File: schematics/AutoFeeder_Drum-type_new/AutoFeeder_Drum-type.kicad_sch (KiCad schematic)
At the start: 35 parts, among them J1 USB_C_Receptacle_6, J2 Conn_02x03_Odd_Even, J3 Conn_01x05, J4 Conn_02x02_Odd_Even, J5 Conn_02x03_Odd_Even, M1 Motor_DC, SW1 SW_SPDT_AND_Push, SW2 SW_DPDT_x2, SW3 SW_DPDT_x2, U1 NJL5901AR-1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

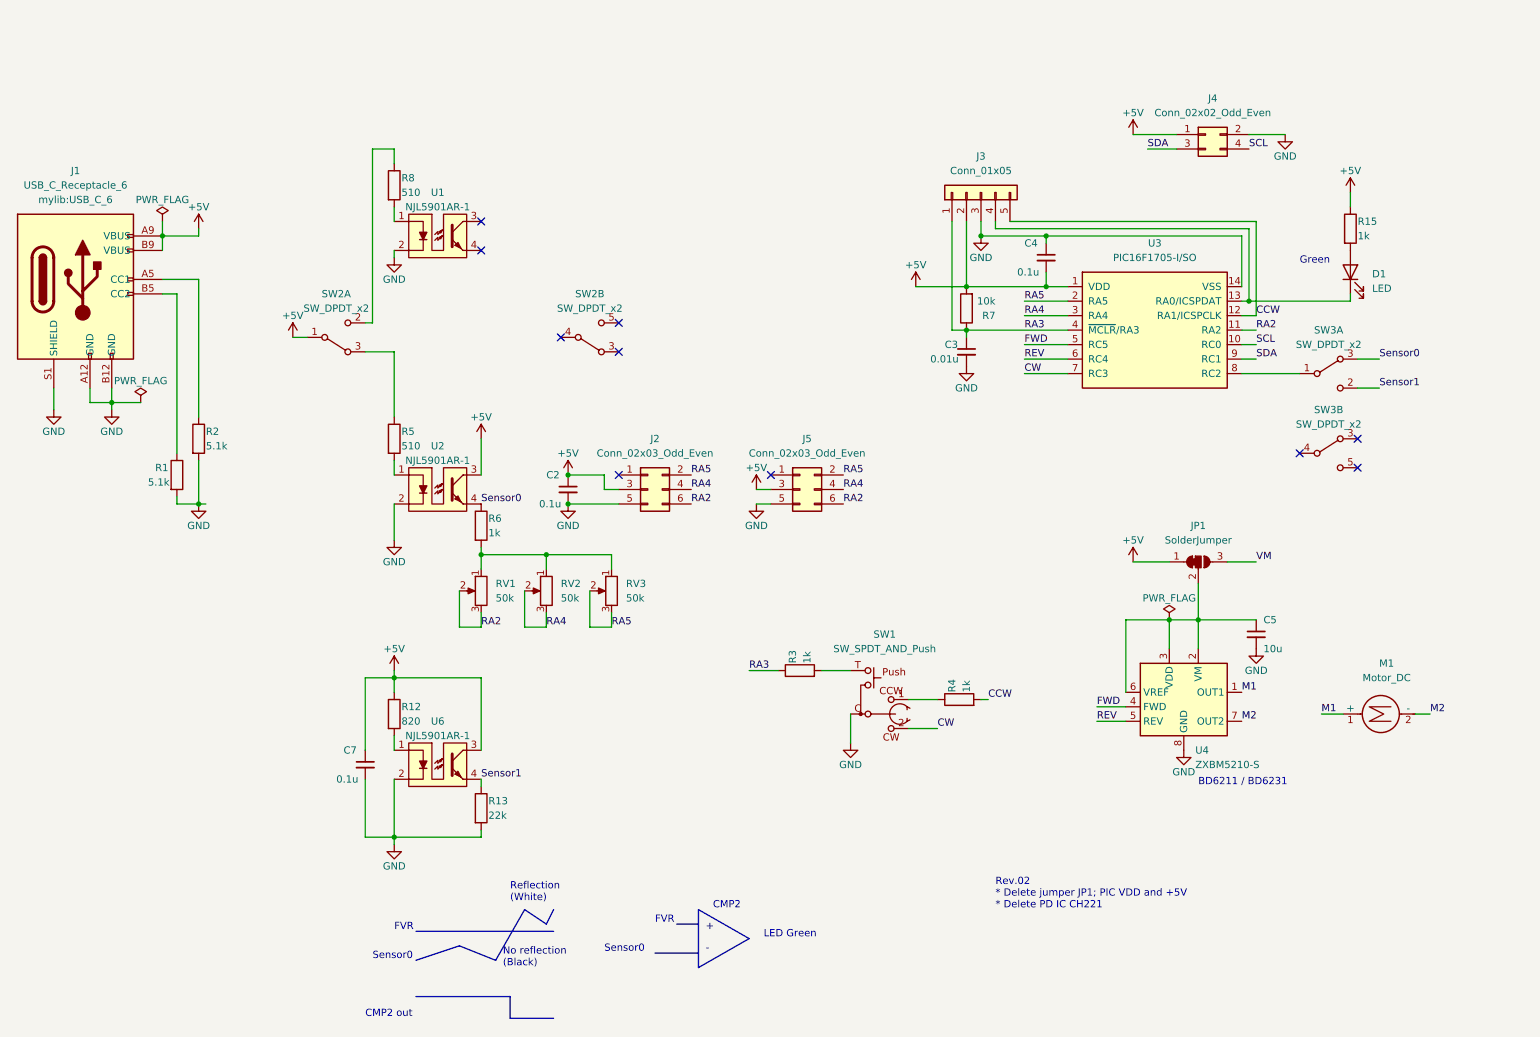
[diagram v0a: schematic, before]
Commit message: Rev.02: Rev01 had a problem with the deep feeder hitting the PCB. Rev02 avoided this problem by overlapping two PCBs for the sensor section.; Three sensitivity options are available for white, transparent, and black feeders.
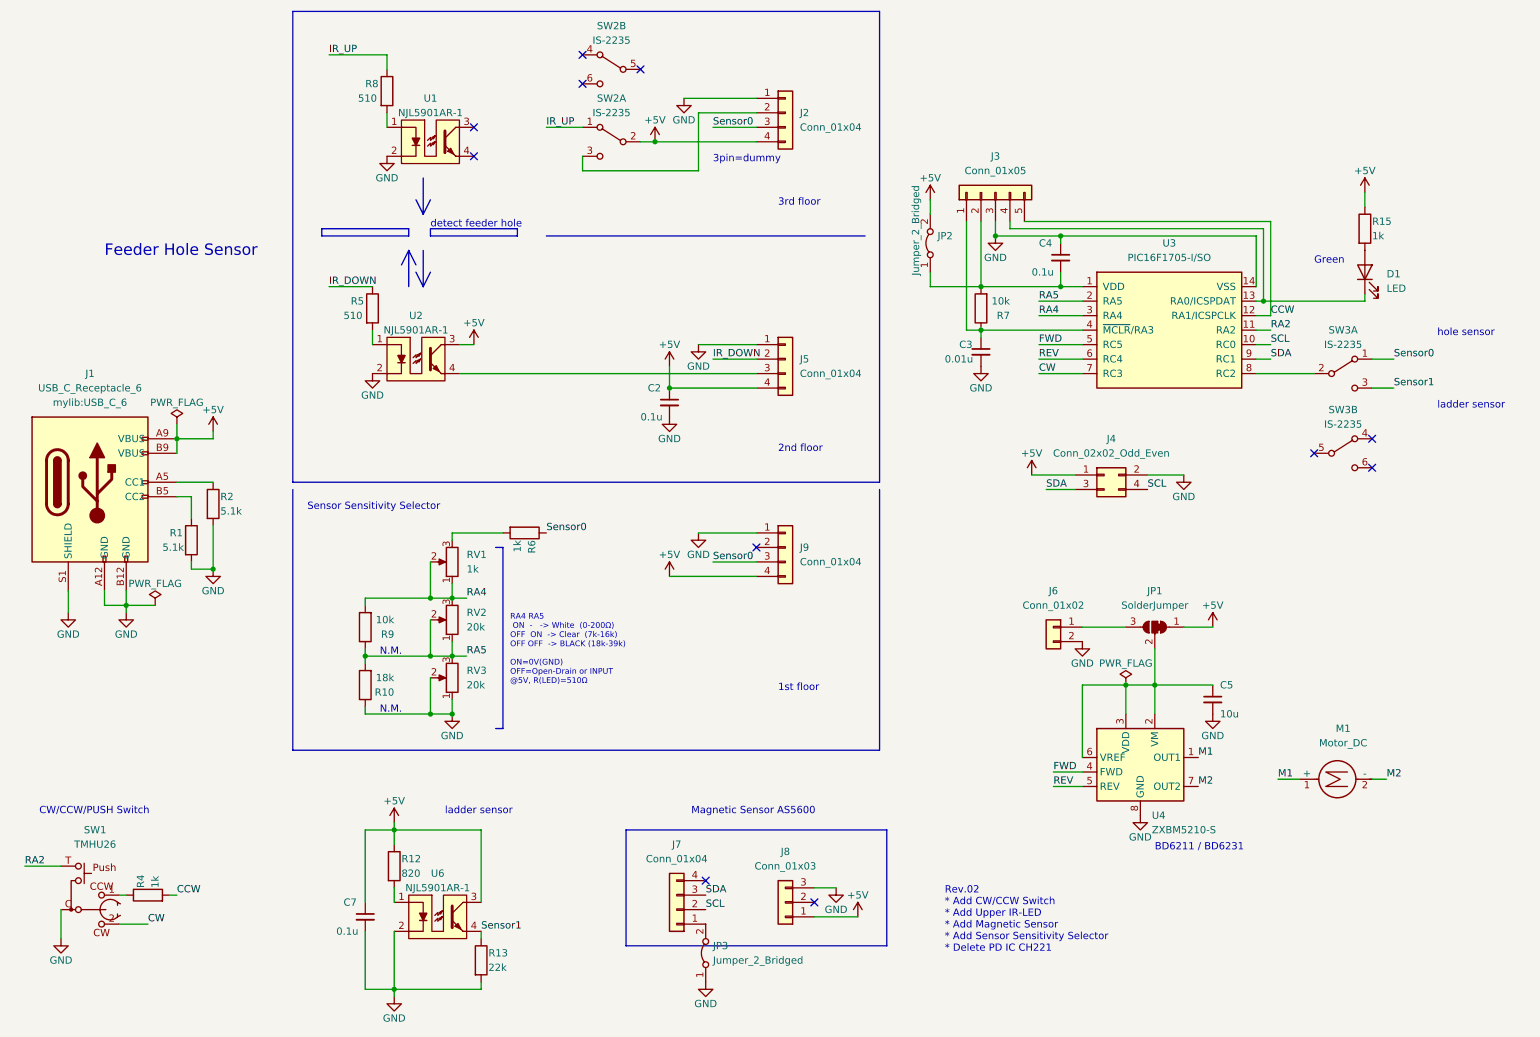
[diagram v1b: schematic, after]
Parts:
- removed J2, J5: Conn_02x03_Odd_Even, symbol Connector_Generic:Conn_02x03_Odd_Even
- removed R3: 1k, Resistor_SMD:R_0603_1608Metric, symbol Device:R
- removed SW2, SW3: SW_DPDT_x2, symbol mylib1:SW_DPDT_x2
- added J2, J5, J7, J9: Conn_01x04, Connector_PinHeader_2.54mm:PinHeader_1x04_P2.54mm_Vertical, symbol Connector_Generic:Conn_01x04
- added J6: Conn_01x02, Connector_JST:JST_XH_B2B-XH-A_1x02_P2.50mm_Vertical, symbol Connector_Generic:Conn_01x02
- added J8: Conn_01x03, Connector_PinHeader_2.54mm:PinHeader_1x03_P2.54mm_Vertical, symbol Connector_Generic:Conn_01x03
- added JP2: Jumper_2_Bridged, Connector_PinHeader_2.54mm:PinHeader_2x01_P2.54mm_Vertical, symbol Jumper:Jumper_2_Bridged
- added JP3: Jumper_2_Bridged, Jumper:SolderJumper-2_P1.3mm_Bridged_RoundedPad1.0x1.5mm, symbol Jumper:Jumper_2_Bridged
- added R10: 18k, Resistor_SMD:R_0603_1608Metric, symbol Device:R
- added R9: 10k, Resistor_SMD:R_0603_1608Metric, symbol Device:R
- added SW2, SW3: IS-2235, mylib:Slide-SW-IS-2235, symbol mylib1:SW_PUSH_DPDT_x2
- RV1: value 50k -> 1k
- RV2, RV3: value 50k -> 20k
- SW1: value SW_SPDT_AND_Push -> TMHU26; footprint (none) -> mylib:THMU26_2
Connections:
- net +5V: now also J2.4 (Pin_4), J5.4 (Pin_4), J8.1 (Pin_1), J9.4 (Pin_4), JP2.2 (B), SW2.2 (B); no longer C4.2, J3.2 (Pin_2), R7.2, U3.1 (VDD)
- net GND: now also RV3.1, RV3.2, J2.1 (Pin_1), J5.1 (Pin_1), J6.2 (Pin_2), J8.3 (Pin_3), J9.1 (Pin_1), JP3.1 (A), R10.1
- net RA2: now also SW1.T; no longer RV1.2, RV1.3
- net RA4: now also RV1.1, RV1.2, R9.2; no longer RV2.2
- net RA5: now also RV2.1, RV2.2, R10.2, R9.1; no longer RV3.2
- net SCL: now also J7.2 (Pin_2)
- net SDA: now also J7.3 (Pin_3)
- net Sensor0: now also J2.3 (Pin_3), J9.3 (Pin_3), SW3.1 (A); no longer U2.4
- net Sensor1: now also SW3.3 (C)
- net IR_UP: now reaches R8.1
- net IR_UP: now also SW2.1 (A)
- net IR_DOWN: now reaches R5.1
- net IR_DOWN: now also J5.2 (Pin_2)
- net at U3.8 (RC2): now also SW3.2 (B)
- net RA3: no longer names the net of C3.1, J3.1 (Pin_1), R7.1, U3.4 (~{MCLR}/RA3)
- net VM: no longer names the net of JP1.3 (B)
- net VM: now also J6.1 (Pin_1)
- new net: R6.2, RV1.3
- new net: J2.2 (Pin_2), SW2.3 (C)
- new net: C4.2, J3.2 (Pin_2), JP2.1 (A), R7.2, U3.1 (VDD)
- new net: J5.3 (Pin_3), U2.4
- new net: J7.1 (Pin_1), JP3.2 (B)
- no-connect marks 10 -> 11
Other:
- note added: "1st floor"
- note added: "2nd floor"
- note added: "3pin=dummy"
- note added: "3rd floor"
- note added: "CW/CCW/PUSH Switch"
- note added: "Feeder Hole Sensor"
- note added: "Magnetic Sensor AS5600"
- note added: "N.M."
- note added: "RA4 RA5 ON - -> White (0-200Ω) OFF ON -> Clear (7k-16k) OFF OFF -> BLACK (18k-39k) ON=0V(GND) OFF=Open-Drain or INPUT @5V, R(LED)=510Ω"
- note added: "Rev.02 * Add CW/CCW Switch * Add Upper IR-LED * Add Magnetic Sensor * Add Sensor Sensitivity Selector * Delete PD IC CH221"
- note added: "Sensor Sensitivity Selector"
- note added: "detect feeder hole"
- note added: "hole sensor"
- note added: "ladder sensor"
- note removed: "+"
- note removed: "-"
- note removed: "CMP2"
- note removed: "CMP2 out"
- note removed: "FVR"
- note removed: "LED Green"
- note removed: "No reflection (Black)"
- note removed: "Reflection (White)"
- note removed: "Rev.02 * Delete jumper JP1; PIC VDD and +5V * Delete PD IC CH221"
- note removed: "Sensor0"
- moved on the sheet: C2, C3, C4, C5, C7, D1, J1, J3, J4, JP1, M1, R1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

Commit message: Change Schematics; Add Red LED for ladder sensor; Add guide line of feeder tape
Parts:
- removed JP3: Jumper_2_Bridged, Jumper:SolderJumper-2_P1.3mm_Bridged_RoundedPad1.0x1.5mm, symbol Jumper:Jumper_2_Bridged
- added D2: LED, LED_SMD:LED_0603_1608Metric, symbol Device:LED
- added JP3: SolderJumper_3_Bridged12, Jumper:SolderJumper-3_P1.3mm_Bridged12_RoundedPad1.0x1.5mm, symbol Jumper:SolderJumper_3_Bridged12
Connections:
- net +5V: now also JP3.3 (B)
- net GND: now also JP3.1 (A)
- net at SW3.4 (A): now also D1.1 (K)
- net at SW3.5 (B): now also J3.4 (Pin_4), U3.13 (RA0/ICSPDAT)
- net at SW3.6 (C): now also D2.1 (K)
- net at D1.2 (A), R15.2: now also D2.2 (A)
- net at J7.1 (Pin_1): now also JP3.2 (C)
- no-connect marks 11 -> 8
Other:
- note added: "Red"
- moved on the sheet: D1, R15, SW3B

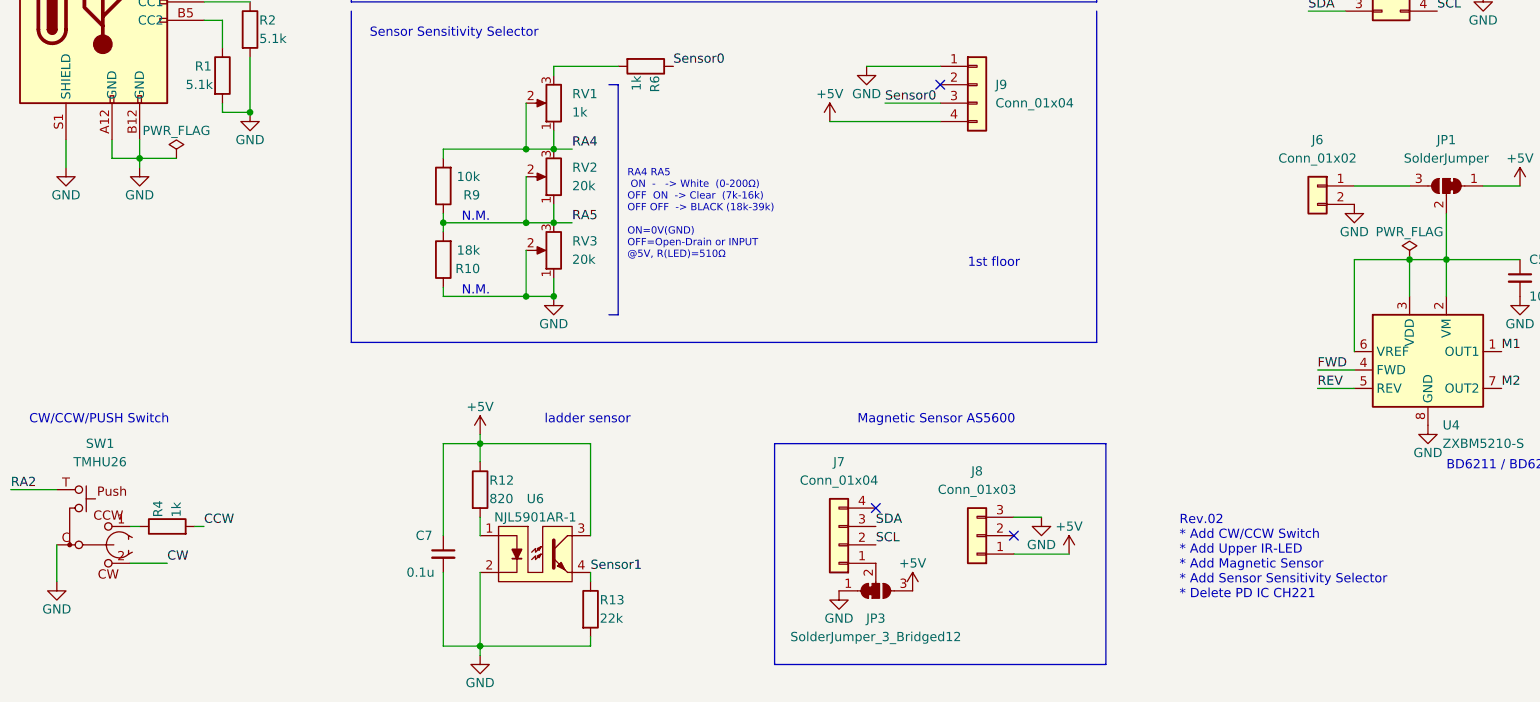
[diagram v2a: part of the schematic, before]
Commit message: Change schematics: Assign CW/CCW pin to connector; Add M3 mounting hole
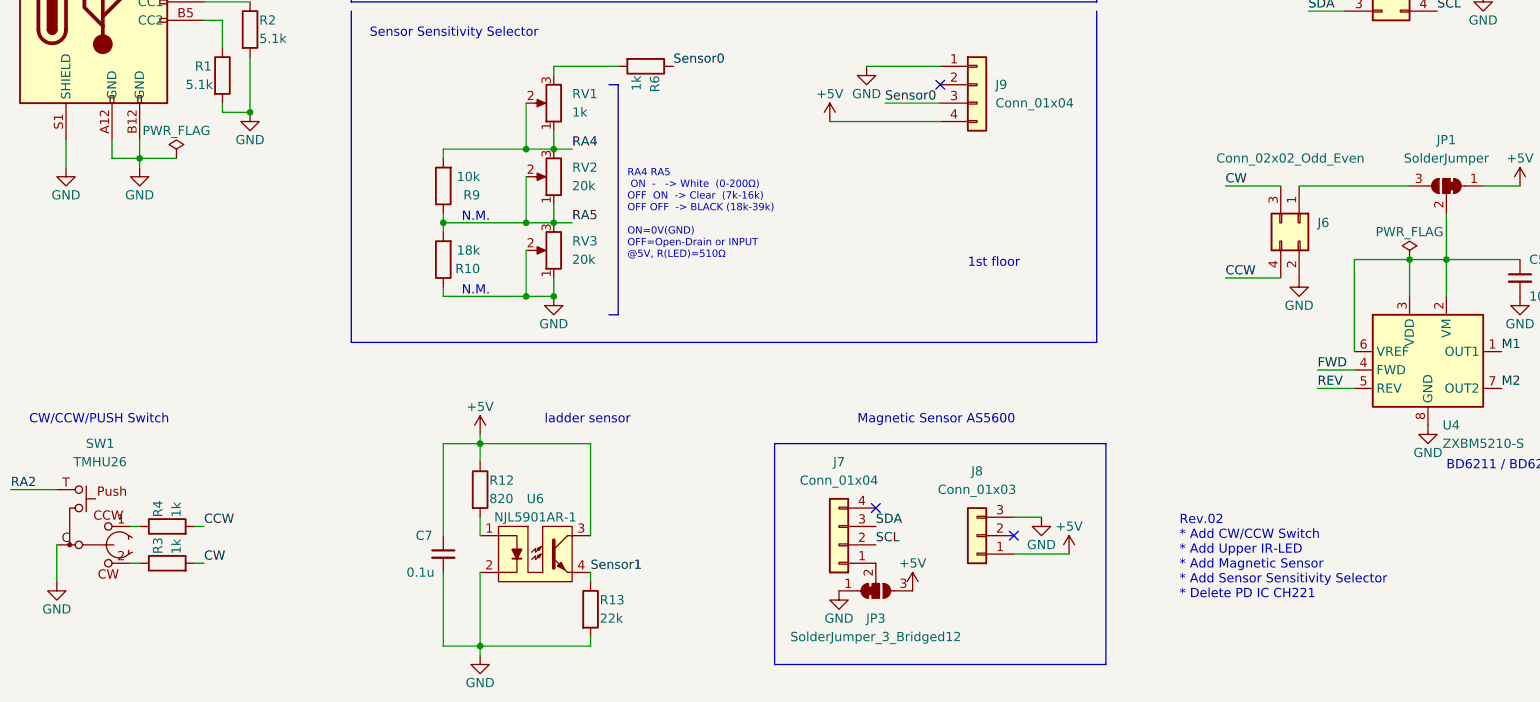
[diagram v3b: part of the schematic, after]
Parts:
- removed J6: Conn_01x02, Connector_JST:JST_XH_B2B-XH-A_1x02_P2.50mm_Vertical, symbol Connector_Generic:Conn_01x02
- added J6: Conn_02x02_Odd_Even, Connector_PinHeader_2.54mm:PinHeader_2x02_P2.54mm_Vertical, symbol Connector_Generic:Conn_02x02_Odd_Even
- added R3: 1k, Resistor_SMD:R_0603_1608Metric, symbol Device:R
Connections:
- net CCW: now also J6.4 (Pin_4)
- net CW: now also J6.3 (Pin_3), R3.2; no longer SW1.2
- net GND: now also J6.2 (Pin_2)
- net at JP1.3 (B): now also J6.1 (Pin_1)
- new net: R3.1, SW1.2
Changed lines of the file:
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@@
+    (stroke (width 0) (type default) (color 0 0 0 0))
+  )
+  (wire (pts (xy 45.72 173.99) (xy 46.99 173.99))
     (stroke (width 0) (type default) (color 0 0 0 0))
   )
@@
     (stroke (width 0) (type default) (color 0 0 0 0))
   )
-  (wire (pts (xy 205.74 121.92) (xy 213.36 121.92))
+  (wire (pts (xy 198.12 121.92) (xy 213.36 121.92))
     (stroke (width 0) (type default) (color 0 0 0 0))
   )
@@
   )
   (wire (pts (xy 218.44 132.08) (xy 228.6 132.08))
+    (stroke (width 0) (type default) (color 0 0 0 0))
+  )
+  (wire (pts (xy 187.96 134.62) (xy 195.58 134.62))
     (stroke (width 0) (type default) (color 0 0 0 0))
   )
@@
     (stroke (width 0) (type solid) (color 0 0 0 0))
   )
+  (wire (pts (xy 187.96 121.92) (xy 195.58 121.92))
+    (stroke (width 0) (type default) (color 0 0 0 0))
+  )
   (wire (pts (xy 198.12 72.39) (xy 205.74 72.39))
     (stroke (width 0) (type default) (color 0 0 0 0))
@@
     (stroke (width 0) (type default) (color 0 0 0 0))
   )
-  (wire (pts (xy 41.91 173.99) (xy 36.83 173.99))
+  (wire (pts (xy 38.1 173.99) (xy 36.83 173.99))
     (stroke (width 0) (type default) (color 0 0 0 0))
   )
@@
     (effects (font (size 1.27 1.27)) (justify left bottom))
   )
+  (label "CW" (at 187.96 121.92 0)
+    (effects (font (size 1.27 1.27)) (justify left bottom))
+  )
   (label "REV" (at 198.12 74.93 0)
     (effects (font (size 1.27 1.27)) (justify left bottom))
@@
     (effects (font (size 1.27 1.27)) (justify left bottom))
   )
+  (label "CCW" (at 187.96 134.62 0)
+    (effects (font (size 1.27 1.27)) (justify left bottom))
+  )
   (label "FWD" (at 200.66 147.32 0)
     (effects (font (size 1.27 1.27)) (justify left bottom))
@@
     (effects (font (size 1.27 1.27)) (justify left bottom))
   )
-  (label "CW" (at 41.91 173.99 0)
+  (label "CW" (at 46.99 173.99 0)
     (effects (font (size 1.27 1.27)) (justify left bottom))
   )
   (label "Sensor0" (at 260.35 74.93 0)
     (effects (font (size 1.27 1.27)) (justify left bottom))
+  )
+  (symbol (lib_id "Connector_Generic:Conn_02x02_Odd_Even") (at 198.12 127 270) (unit 1)
+    (in_bom yes) (on_board yes)
+    (property "Reference" "J6" (id 0) (at 200.66 126.9999 90)
+      (effects (font (size 1.27 1.27)) (justify left))
+    )
+    (property "Value" "Conn_02x02_Odd_Even" (id 1) (at 186.69 118.11 90)
+      (effects (font (size 1.27 1.27)) (justify left))
+    )
+    (property "Footprint" "Connector_PinHeader_2.54mm:PinHeader_2x02_P2.54mm_Vertical" (id 2) (at 198.12 127 0)
+      (effects (font (size 1.27 1.27)) hide)
+    )
+    (property "Datasheet" "~" (id 3) (at 198.12 127 0)
+      (effects (font (size 1.27 1.27)) hide)
+    )
+    (pin "1")
+    (pin "2")
+    (pin "3")
+    (pin "4")
   )
   (symbol (lib_id "Device:R") (at 107.95 105.41 270) (unit 1)
@@
     (pin "3")
   )
-  (symbol (lib_id "Connector_Generic:Conn_01x02") (at 200.66 121.92 0) (mirror y) (unit 1)
-    (in_bom yes) (on_board yes) (fields_autoplaced)
-    (property "Reference" "J6" (id 0) (at 200.66 115.57 0))
-    (property "Value" "Conn_01x02" (id 1) (at 200.66 118.11 0))
-    (property "Footprint" "Connector_JST:JST_XH_B2B-XH-A_1x02_P2.50mm_Vertical" (id 2) (at 200.66 121.92 0)
-      (effects (font (size 1.27 1.27)) hide)
-    )
-    (property "Datasheet" "~" (id 3) (at 200.66 121.92 0)
-      (effects (font (size 1.27 1.27)) hide)
-    )
-    (pin "1")
-    (pin "2")
-  )
   (symbol (lib_id "power:GND") (at 135.89 29.21 0) (unit 1)
     (in_bom yes) (on_board yes)
@@
     (pin "1")
   )
-  (symbol (lib_id "power:GND") (at 205.74 124.46 0) (unit 1)
-    (in_bom yes) (on_board yes)
-    (property "Reference" "#PWR019" (id 0) (at 205.74 130.81 0)
-      (effects (font (size 1.27 1.27)) hide)
-    )
-    (property "Value" "GND" (id 1) (at 205.74 128.27 0))
-    (property "Footprint" "" (id 2) (at 205.74 124.46 0)
-      (effects (font (size 1.27 1.27)) hide)
-    )
-    (property "Datasheet" "" (id 3) (at 205.74 124.46 0)
+  (symbol (lib_id "power:GND") (at 198.12 134.62 0) (unit 1)
+    (in_bom yes) (on_board yes)
+    (property "Reference" "#PWR019" (id 0) (at 198.12 140.97 0)
+      (effects (font (size 1.27 1.27)) hide)
+    )
+    (property "Value" "GND" (id 1) (at 198.12 138.43 0))
+    (property "Footprint" "" (id 2) (at 198.12 134.62 0)
+      (effects (font (size 1.27 1.27)) hide)
+    )
+    (property "Datasheet" "" (id 3) (at 198.12 134.62 0)
       (effects (font (size 1.27 1.27)) hide)
     )
@@
     )
     (property "Datasheet" "~" (id 3) (at 256.54 46.99 0)
+      (effects (font (size 1.27 1.27)) hide)
+    )
+    (pin "1")
+    (pin "2")
+  )
+  (symbol (lib_id "Device:R") (at 41.91 173.99 90) (unit 1)
+    (in_bom yes) (on_board yes)
+    (property "Reference" "R3" (id 0) (at 40.64 172.72 0)
+      (effects (font (size 1.27 1.27)) (justify left))
+    )
+    (property "Value" "1k" (id 1) (at 43.18 172.72 0)
+      (effects (font (size 1.27 1.27)) (justify left))
+    )
+    (property "Footprint" "Resistor_SMD:R_0603_1608Metric" (id 2) (at 41.91 175.768 90)
+      (effects (font (size 1.27 1.27)) hide)
+    )
+    (property "Datasheet" "~" (id 3) (at 41.91 173.99 0)
       (effects (font (size 1.27 1.27)) hide)
     )
@@
       (reference "J5") (unit 1) (value "Conn_01x04") (footprint "Connector_PinHeader_2.54mm:PinHeader_1x04_P2.54mm_Vertical")
     )
-    (path "/9360c59e-a14f-4fbd-99b5-8ae26c93450b"
-      (reference "J6") (unit 1) (value "Conn_01x02") (footprint "Connector_JST:JST_XH_B2B-XH-A_1x02_P2.50mm_Vertical")
+    (path "/06161094-4bc5-40fc-8876-0dc0fd47eb89"
+      (reference "J6") (unit 1) (value "Conn_02x02_Odd_Even") (footprint "Connector_PinHeader_2.54mm:PinHeader_2x02_P2.54mm_Vertical")
     )
     (path "/b635d2c1-9675-4c71-b0c4-4bae6007c9fe"
@@
       (reference "R2") (unit 1) (value "5.1k") (footprint "Resistor_SMD:R_0603_1608Metric")
     )
+    (path "/b4115d81-b868-487b-aa67-bef8491b5649"
+      (reference "R3") (unit 1) (value "1k") (footprint "Resistor_SMD:R_0603_1608Metric")
+    )
     (path "/a583dddb-ff3b-4ea5-86bb-ba6d25742e1f"
